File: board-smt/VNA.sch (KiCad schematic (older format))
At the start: 68 parts, among them J1 Conn_02x05_Odd_Even, J10 Conn_01x01, J11 Conn_01x01, J12 Conn_01x01, J13 Barrel_Jack, J15 Conn_02x05_Odd_Even, J17 Conn_01x04, J18 Conn_01x01, J19 Conn_01x01, J2 Conn_Coaxial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

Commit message: Changed SMA connector, added dual power option for LCD
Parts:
- removed Q1: SS9018, TO_SOT_Packages_THT:TO-92_Molded_Narrow, symbol 2N3904
- added C41: 100 nF, Capacitors_SMD:C_0805_HandSoldering, symbol C_Small
- added JP5: Jumper_NC_Dual, Pin_Headers:Pin_Header_Straight_1x03_Pitch2.54mm, symbol Jumper_NC_Dual
- added Q3: S9018, TO_SOT_Packages_SMD:SOT-23, symbol MMBT3904
- added U8: AMS1117-3V3, TO_SOT_Packages_SMD:SOT-223, symbol AMS1117-3V3
- U9: value LM7805_TO220 -> 78M05_TO252
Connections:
- wire segments 202 -> 212

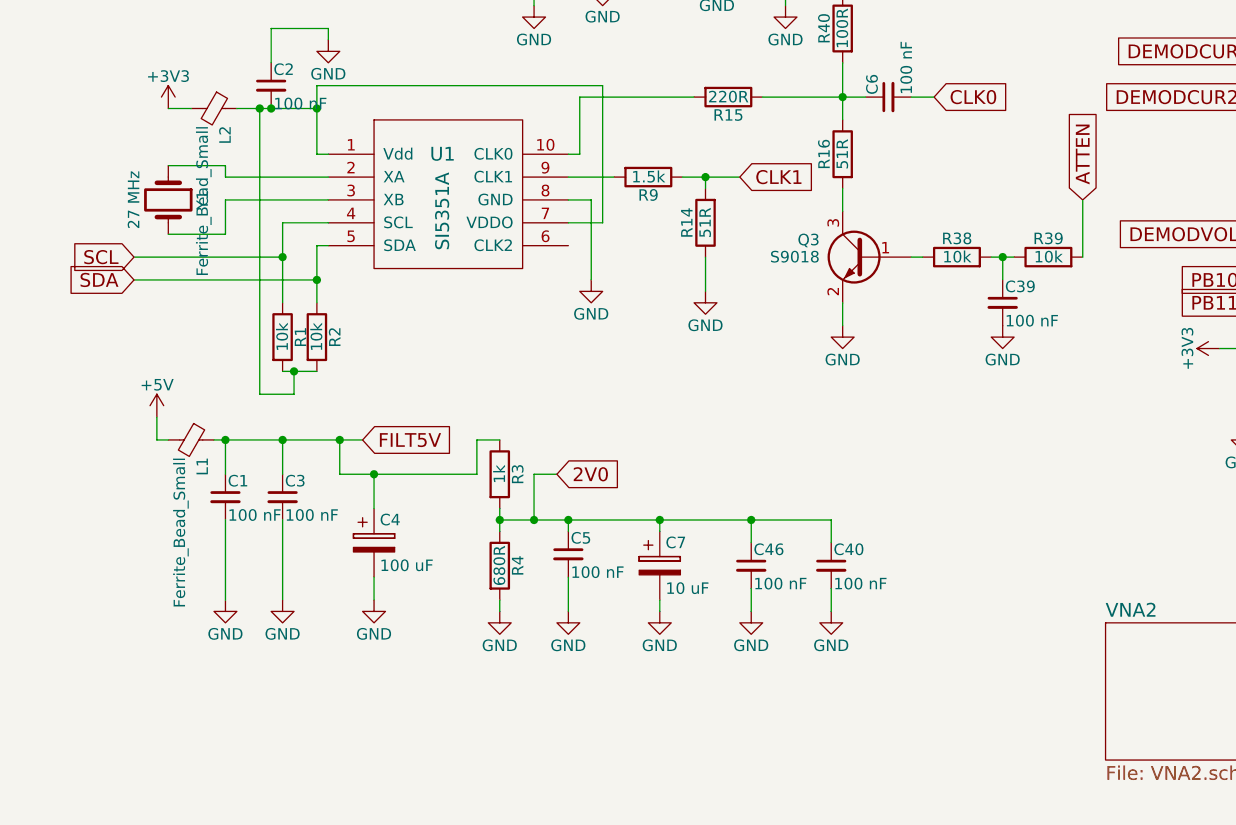
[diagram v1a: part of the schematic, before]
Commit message: Increased isolation between ports
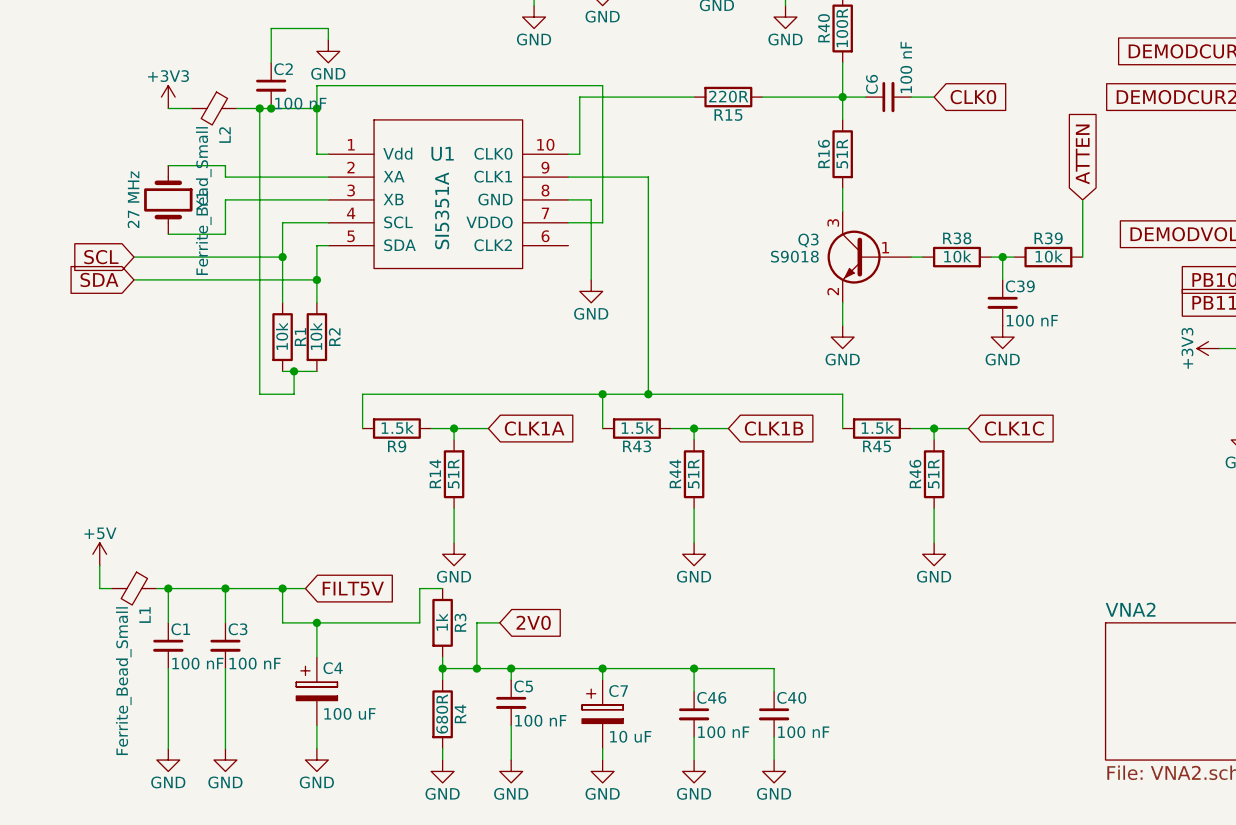
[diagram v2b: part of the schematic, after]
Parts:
- added R43, R45: 1.5k, Resistors_SMD:R_0805_HandSoldering, symbol R
- added R44, R46: 51R, Resistors_SMD:R_0805_HandSoldering, symbol R
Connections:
- net GND: now also R44.1, R46.1
- net at R9.2, U1.9 (CLK1): now also R43.2, R45.2
- net CLK1 renamed CLK1A
- new net CLK1B: R43.1, R44.2
- new net CLK1C: R45.1, R46.2
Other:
- moved on the sheet: C1, C3, C4, C40, C46, C5, C7, L1, R14, R3, R4, R9

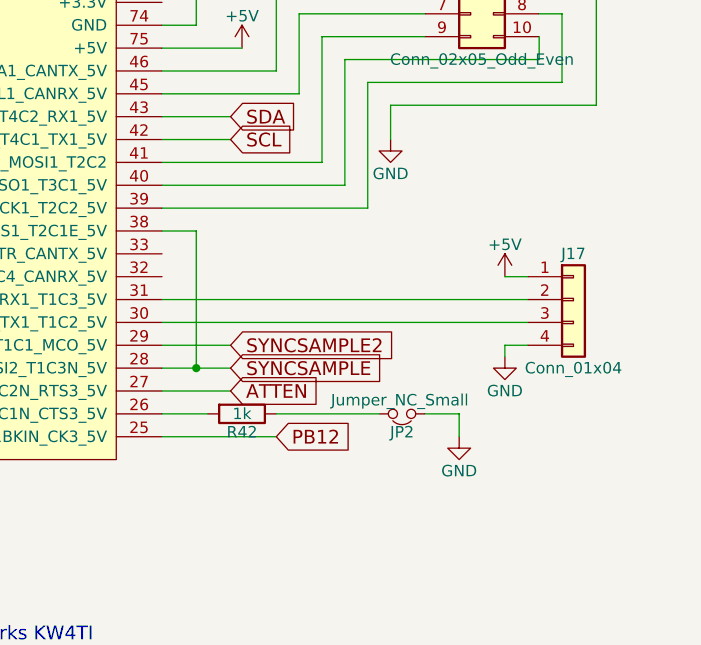
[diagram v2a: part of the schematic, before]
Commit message: Added ferrite beads to serial connection
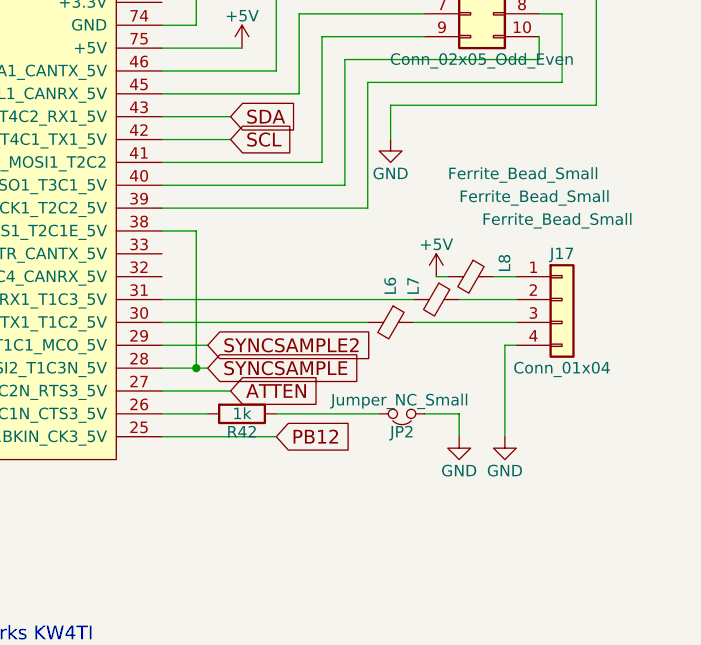
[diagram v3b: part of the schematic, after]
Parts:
- added L6, L7, L8: Ferrite_Bead_Small, Inductors_SMD:L_0805_HandSoldering, symbol Ferrite_Bead_Small
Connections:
- net +5V: now also L8.2; no longer J17.1 (Pin_1)
- net at UB1.30 (PA9_TX1_T1C2_5V): now also L6.2; no longer J17.3 (Pin_3)
- net at UB1.31 (PA10_RX1_T1C3_5V): now also L7.2; no longer J17.2 (Pin_2)
- new net: J17.1 (Pin_1), L8.1
- new net: J17.2 (Pin_2), L7.1
- new net: J17.3 (Pin_3), L6.1
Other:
- moved on the sheet: J17

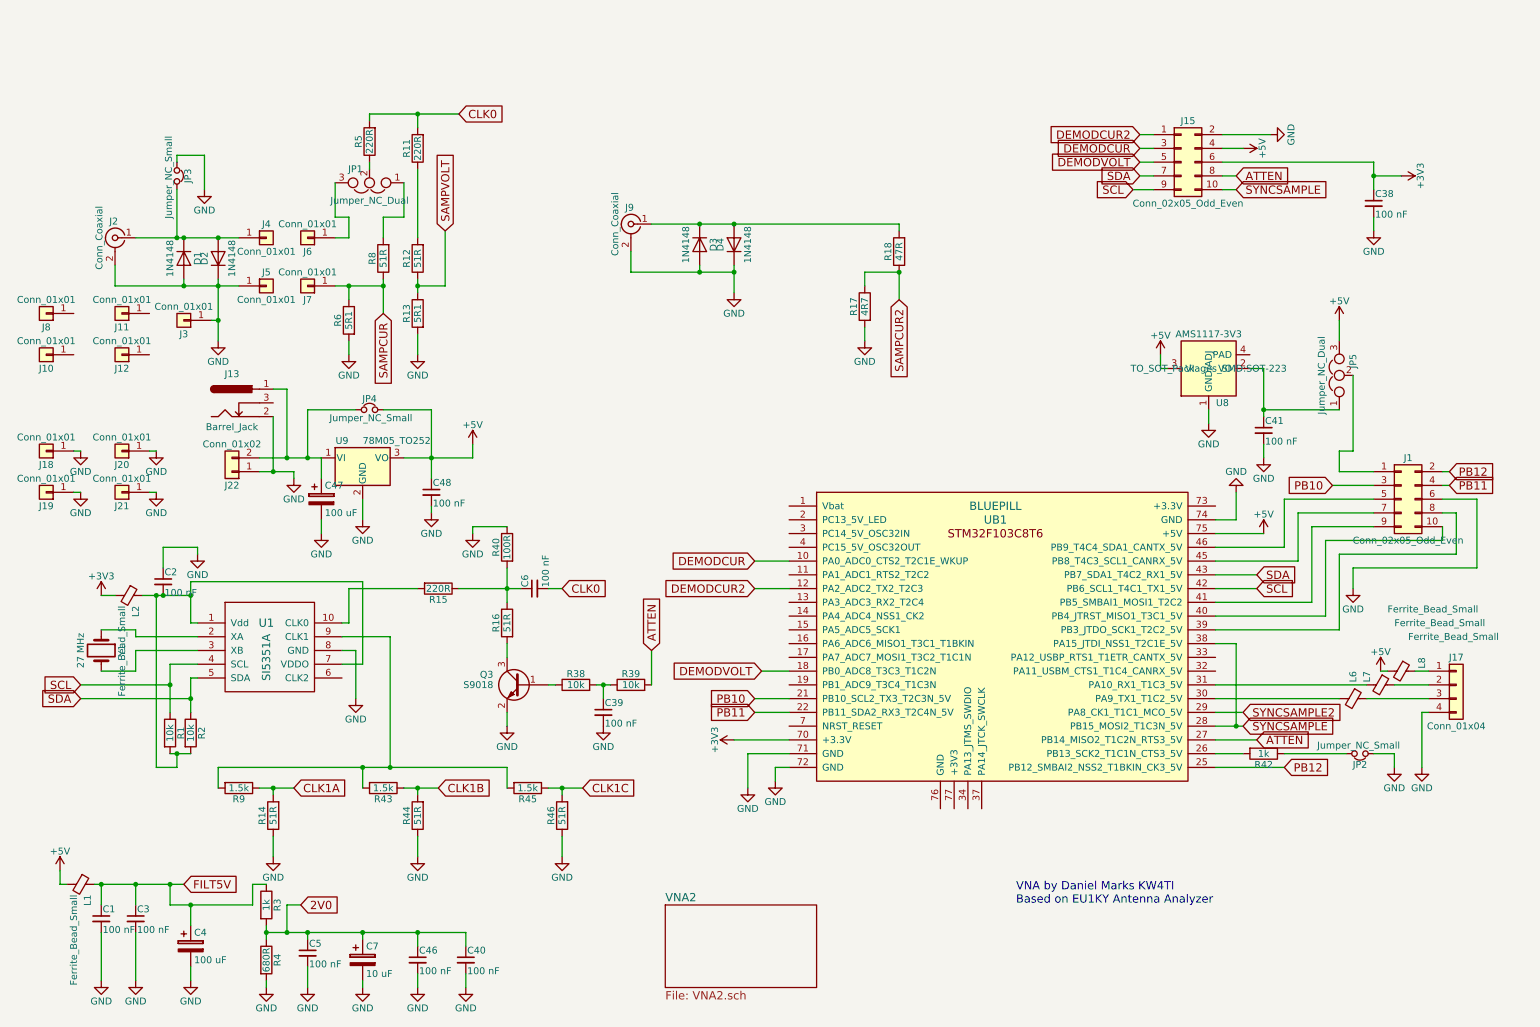
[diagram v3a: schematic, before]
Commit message: Added extra outputs to connector, changed display off pin
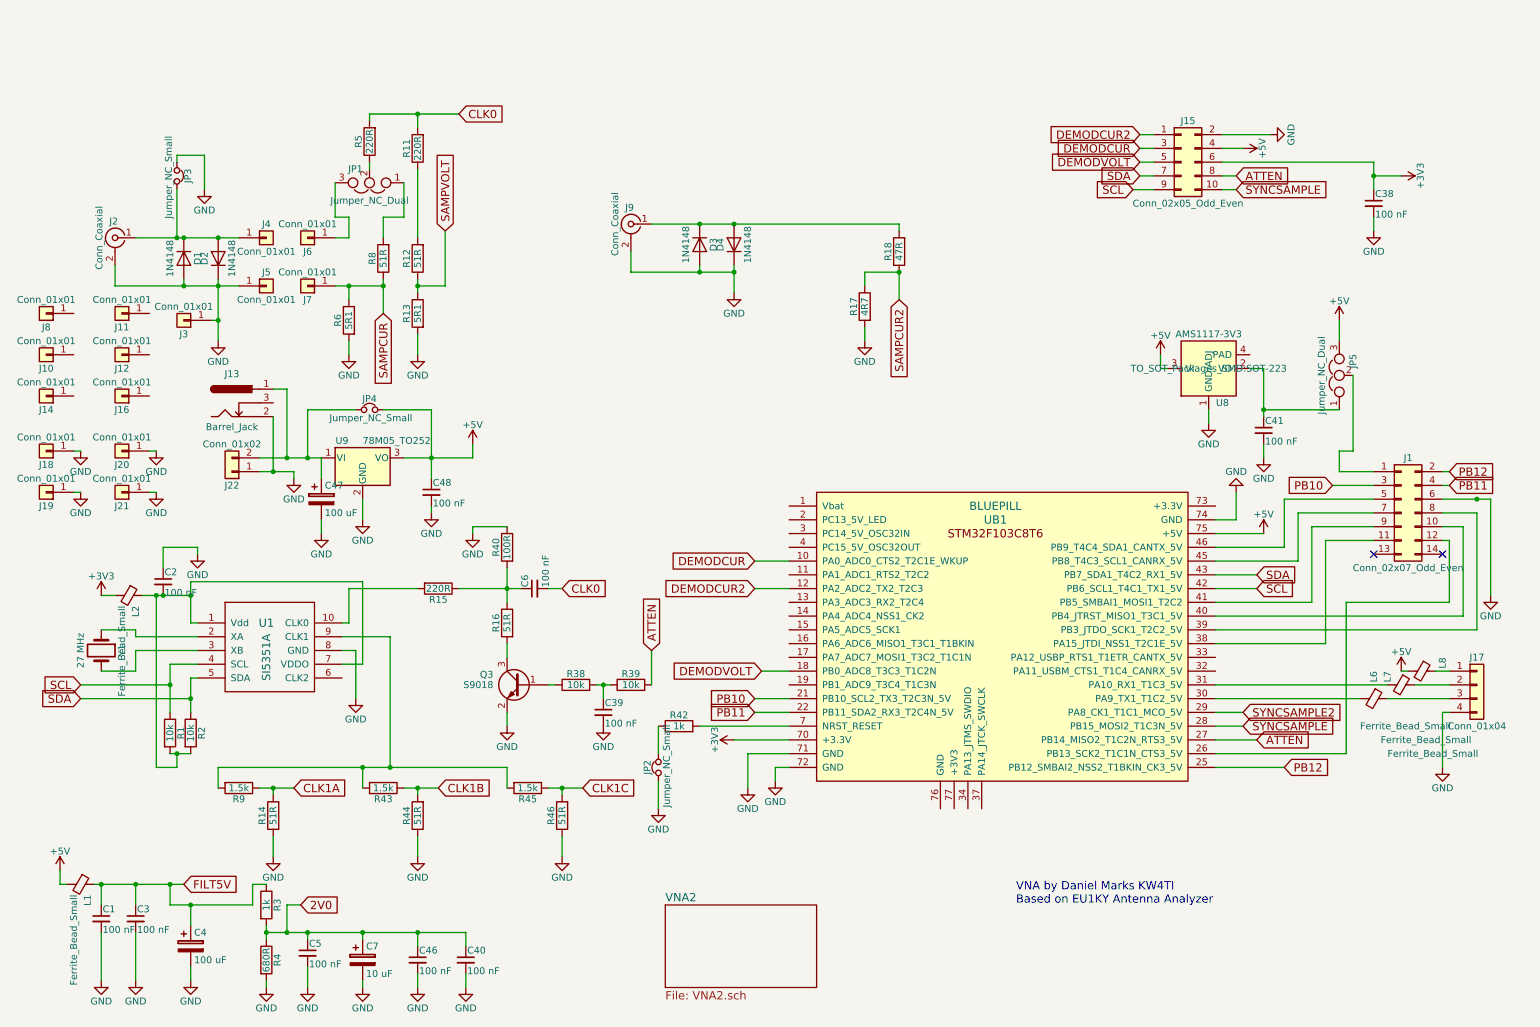
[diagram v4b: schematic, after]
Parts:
- removed J1: Conn_02x05_Odd_Even, Pin_Headers:Pin_Header_Straight_2x05_Pitch2.54mm, symbol Conn_02x05_Odd_Even
- added J1: Conn_02x07_Odd_Even, Pin_Headers:Pin_Header_Straight_2x07_Pitch2.54mm, symbol Conn_02x07_Odd_Even
- added J14, J16: Conn_01x01, Connectors:1pin, symbol Conn_01x01
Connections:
- net GND: now also J1.6 (Pin_6)
- net PB10: now also J1.3 (Pin_3)
- net PB11: now also J1.4 (Pin_4)
- net PB12: now also J1.2 (Pin_2)
- net SYNCSAMPLE: no longer UB1.38 (PA15_JTDI_NSS1_T2C1E_5V)
- net at UB1.26 (PB13_SCK2_T1C1N_CTS3_5V): now also J1.12 (Pin_12); no longer R42.2
- net at UB1.39 (PB3_JTDO_SCK1_T2C2_5V): now also J1.8 (Pin_8)
- net at UB1.40 (PB4_JTRST_MISO1_T3C1_5V): now also J1.10 (Pin_10)
- net at UB1.41 (PB5_SMBAI1_MOSI1_T2C2): now also J1.9 (Pin_9)
- net at UB1.45 (PB8_T4C3_SCL1_CANRX_5V): now also J1.7 (Pin_7)
- net at UB1.46 (PB9_T4C4_SDA1_CANTX_5V): now also J1.5 (Pin_5)
- net at UB1.7 (NRST_RESET): now also R42.2
- net at JP5.2: now also J1.1 (Pin_1)
- new net: J1.11 (Pin_11), UB1.38 (PA15_JTDI_NSS1_T2C1E_5V)
- no-connect marks 0 -> 2
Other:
- moved on the sheet: J17, JP2, L6, L7, L8, R42

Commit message: Daughterboard added for jog wheel and buttons
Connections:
- net at UB1.19 (PB1_ADC9_T3C4_T1C3N): now also R42.2
- net at UB1.7 (NRST_RESET): no longer R42.2
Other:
- moved on the sheet: R42
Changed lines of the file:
@@
 L R R42
 U 1 1 5C1BD47E
-P 5300 5600
-F 0 "R42" V 5380 5600 50  0000 C CNN
-F 1 "1k" V 5300 5600 50  0000 C CNN
-F 2 "Resistors_SMD:R_0805_HandSoldering" V 5230 5600 50  0001 C CNN
-F 3 "" H 5300 5600 50  0001 C CNN
-	1    5300 5600
+P 5350 5300
+F 0 "R42" V 5430 5300 50  0000 C CNN
+F 1 "1k" V 5350 5300 50  0000 C CNN
+F 2 "Resistors_SMD:R_0805_HandSoldering" V 5280 5300 50  0001 C CNN
+F 3 "" H 5350 5300 50  0001 C CNN
+	1    5350 5300
 	0    -1   -1   0
 $EndComp
@@
 $EndComp
 Wire Wire Line
-	6100 5600 5450 5600
-Wire Wire Line
-	5150 5800 5150 5600
+	5150 5300 5150 5800
 Wire Wire Line
 	5150 6200 5150 6000
@@
 Wire Wire Line
 	10150 5800 9200 5800
+Wire Wire Line
+	5500 5300 6100 5300
+Wire Wire Line
+	5150 5300 5200 5300
 $EndSCHEMATC

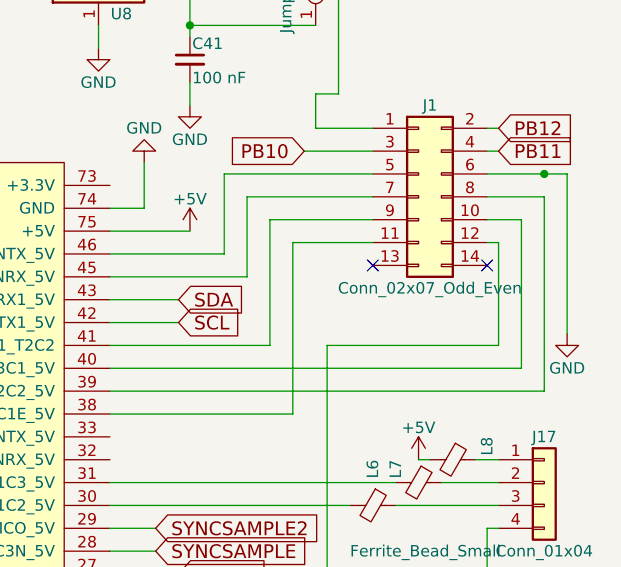
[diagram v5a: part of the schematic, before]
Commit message: Added vacuum holes to fixture
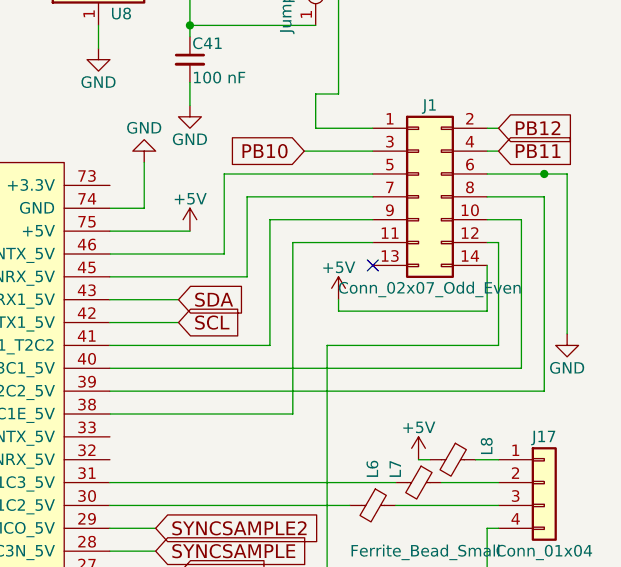
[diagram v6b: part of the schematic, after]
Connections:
- net +5V: now also J1.14 (Pin_14)
- no-connect marks 2 -> 1
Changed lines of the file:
@@
 	11000 4150 10850 4150
 NoConn ~ 10350 4350
-NoConn ~ 10850 4350
 Wire Wire Line
 	10150 5800 9200 5800
@@
 Wire Wire Line
 	5150 5300 5200 5300
+$Comp
+L +5V #PWR?
+U 1 1 5DB1C7B8
+P 10200 4500
+F 0 "#PWR?" H 10200 4350 50  0001 C CNN
+F 1 "+5V" H 10200 4640 50  0000 C CNN
+F 2 "" H 10200 4500 50  0001 C CNN
+F 3 "" H 10200 4500 50  0001 C CNN
+	1    10200 4500
+	1    0    0    -1
+$EndComp
+Wire Wire Line
+	10850 4350 10850 4550
+Wire Wire Line
+	10850 4550 10200 4550
+Wire Wire Line
+	10200 4550 10200 4500
 $EndSCHEMATC
